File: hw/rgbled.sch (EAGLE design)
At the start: 14 parts, among them IC1 LE33CZ, Q1 IRLZ34N, Q2 IRLZ34N, Q3 IRLZ34N, U1 ATTINY85-20P, X1 22-23-2021

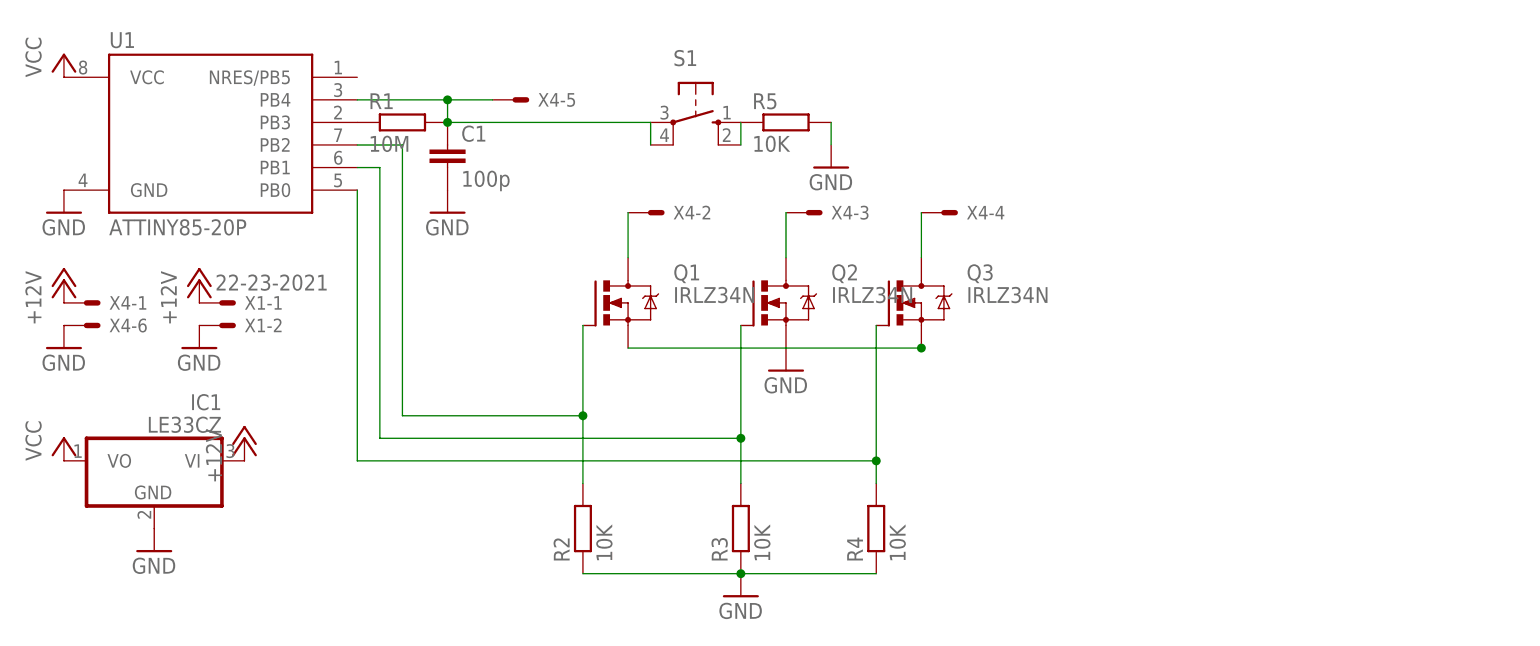
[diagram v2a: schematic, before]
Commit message: upravy problikavani
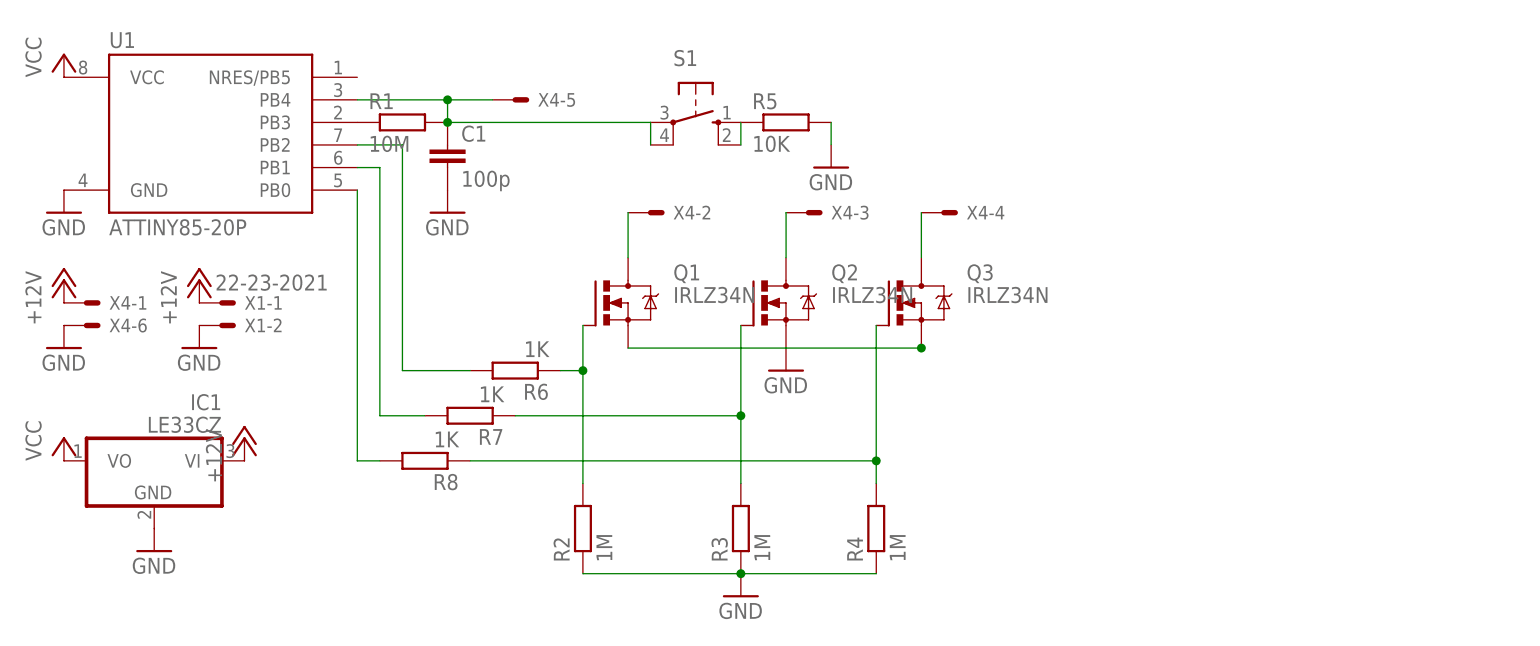
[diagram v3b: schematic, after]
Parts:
- added R6, R7, R8: 1K, resistor:R-EU_0204/5
- R2, R3, R4: value 10K -> 1M
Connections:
- new net N$6: Q1.G, R2.2, R6.1
- new net N$8: Q2.G, R3.2, R7.1
- new net N$9: Q3.G, R4.2, R8.1
- net N$10: now also R8.2; no longer Q3.G, R4.2
- net N$11: now also R7.2; no longer Q2.G, R3.2
- net N$12: now also R6.2; no longer Q1.G, R2.2
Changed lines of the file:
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@@
 <part name="C1" library="resistor" deviceset="C-EU" device="025-024X044" value="100p"/>
 <part name="GND6" library="supply1" deviceset="GND" device=""/>
-<part name="R2" library="resistor" deviceset="R-EU_" device="0204/5" value="10K"/>
-<part name="R3" library="resistor" deviceset="R-EU_" device="0204/5" value="10K"/>
-<part name="R4" library="resistor" deviceset="R-EU_" device="0204/5" value="10K"/>
+<part name="R2" library="resistor" deviceset="R-EU_" device="0204/5" value="1M"/>
+<part name="R3" library="resistor" deviceset="R-EU_" device="0204/5" value="1M"/>
+<part name="R4" library="resistor" deviceset="R-EU_" device="0204/5" value="1M"/>
 <part name="GND7" library="supply1" deviceset="GND" device=""/>
 <part name="S1" library="switch-omron" deviceset="10-XX" device=""/>
 <part name="GND8" library="supply1" deviceset="GND" device=""/>
 <part name="R5" library="resistor" deviceset="R-EU_" device="0204/5" value="10K"/>
+<part name="R6" library="resistor" deviceset="R-EU_" device="0204/5" value="1K"/>
+<part name="R7" library="resistor" deviceset="R-EU_" device="0204/5" value="1K"/>
+<part name="R8" library="resistor" deviceset="R-EU_" device="0204/5" value="1K"/>
 </parts>
 <sheets>
@@
 <instance part="GND8" gate="1" x="93.98" y="53.34"/>
 <instance part="R5" gate="G$1" x="88.9" y="58.42"/>
+<instance part="R6" gate="G$1" x="58.42" y="30.48" rot="R180"/>
+<instance part="R7" gate="G$1" x="53.34" y="25.4" rot="R180"/>
+<instance part="R8" gate="G$1" x="48.26" y="20.32" rot="R180"/>
 </instances>
 <busses>
@@
 <net name="N$10" class="0">
 <segment>
-<pinref part="Q3" gate="G$1" pin="G"/>
-<wire x1="99.06" y1="35.56" x2="99.06" y2="20.32" width="0.1524" layer="91"/>
-<pinref part="R4" gate="G$1" pin="2"/>
 <pinref part="U1" gate="G$1" pin="PB0"/>
-<wire x1="99.06" y1="20.32" x2="99.06" y2="17.78" width="0.1524" layer="91"/>
-<wire x1="99.06" y1="20.32" x2="40.64" y2="20.32" width="0.1524" layer="91"/>
 <wire x1="40.64" y1="20.32" x2="40.64" y2="50.8" width="0.1524" layer="91"/>
-<junction x="99.06" y="20.32"/>
+<pinref part="R8" gate="G$1" pin="2"/>
+<wire x1="40.64" y1="20.32" x2="43.18" y2="20.32" width="0.1524" layer="91"/>
 </segment>
 </net>
 <net name="N$11" class="0">
 <segment>
-<pinref part="Q2" gate="G$1" pin="G"/>
-<wire x1="83.82" y1="35.56" x2="83.82" y2="22.86" width="0.1524" layer="91"/>
-<pinref part="R3" gate="G$1" pin="2"/>
-<wire x1="83.82" y1="22.86" x2="83.82" y2="17.78" width="0.1524" layer="91"/>
-<wire x1="83.82" y1="22.86" x2="43.18" y2="22.86" width="0.1524" layer="91"/>
-<wire x1="43.18" y1="22.86" x2="43.18" y2="53.34" width="0.1524" layer="91"/>
 <pinref part="U1" gate="G$1" pin="PB1"/>
 <wire x1="43.18" y1="53.34" x2="40.64" y2="53.34" width="0.1524" layer="91"/>
-<junction x="83.82" y="22.86"/>
+<wire x1="43.18" y1="53.34" x2="43.18" y2="25.4" width="0.1524" layer="91"/>
+<pinref part="R7" gate="G$1" pin="2"/>
+<wire x1="43.18" y1="25.4" x2="48.26" y2="25.4" width="0.1524" layer="91"/>
 </segment>
 </net>
 <net name="N$12" class="0">
 <segment>
-<pinref part="Q1" gate="G$1" pin="G"/>
-<wire x1="66.04" y1="35.56" x2="66.04" y2="25.4" width="0.1524" layer="91"/>
-<pinref part="R2" gate="G$1" pin="2"/>
-<wire x1="66.04" y1="25.4" x2="66.04" y2="17.78" width="0.1524" layer="91"/>
-<wire x1="66.04" y1="25.4" x2="45.72" y2="25.4" width="0.1524" layer="91"/>
-<wire x1="45.72" y1="25.4" x2="45.72" y2="55.88" width="0.1524" layer="91"/>
 <pinref part="U1" gate="G$1" pin="PB2"/>
 <wire x1="45.72" y1="55.88" x2="40.64" y2="55.88" width="0.1524" layer="91"/>
-<junction x="66.04" y="25.4"/>
+<wire x1="45.72" y1="55.88" x2="45.72" y2="30.48" width="0.1524" layer="91"/>
+<pinref part="R6" gate="G$1" pin="2"/>
+<wire x1="45.72" y1="30.48" x2="53.34" y2="30.48" width="0.1524" layer="91"/>
 </segment>
 </net>
@@
 </segment>
 </net>
+<net name="N$8" class="0">
+<segment>
+<pinref part="Q2" gate="G$1" pin="G"/>
+<wire x1="83.82" y1="35.56" x2="83.82" y2="25.4" width="0.1524" layer="91"/>
+<pinref part="R3" gate="G$1" pin="2"/>
+<pinref part="R7" gate="G$1" pin="1"/>
+<wire x1="83.82" y1="25.4" x2="83.82" y2="17.78" width="0.1524" layer="91"/>
+<wire x1="58.42" y1="25.4" x2="83.82" y2="25.4" width="0.1524" layer="91"/>
+<junction x="83.82" y="25.4"/>
+</segment>
+</net>
+<net name="N$9" class="0">
+<segment>
+<pinref part="Q3" gate="G$1" pin="G"/>
+<wire x1="99.06" y1="35.56" x2="99.06" y2="20.32" width="0.1524" layer="91"/>
+<pinref part="R4" gate="G$1" pin="2"/>
+<pinref part="R8" gate="G$1" pin="1"/>
+<wire x1="99.06" y1="20.32" x2="99.06" y2="17.78" width="0.1524" layer="91"/>
+<wire x1="53.34" y1="20.32" x2="99.06" y2="20.32" width="0.1524" layer="91"/>
+<junction x="99.06" y="20.32"/>
+</segment>
+</net>
+<net name="N$6" class="0">
+<segment>
+<pinref part="Q1" gate="G$1" pin="G"/>
+<pinref part="R2" gate="G$1" pin="2"/>
+<wire x1="66.04" y1="35.56" x2="66.04" y2="30.48" width="0.1524" layer="91"/>
+<pinref part="R6" gate="G$1" pin="1"/>
+<wire x1="66.04" y1="30.48" x2="66.04" y2="17.78" width="0.1524" layer="91"/>
+<wire x1="63.5" y1="30.48" x2="66.04" y2="30.48" width="0.1524" layer="91"/>
+<junction x="66.04" y="30.48"/>
+</segment>
+</net>

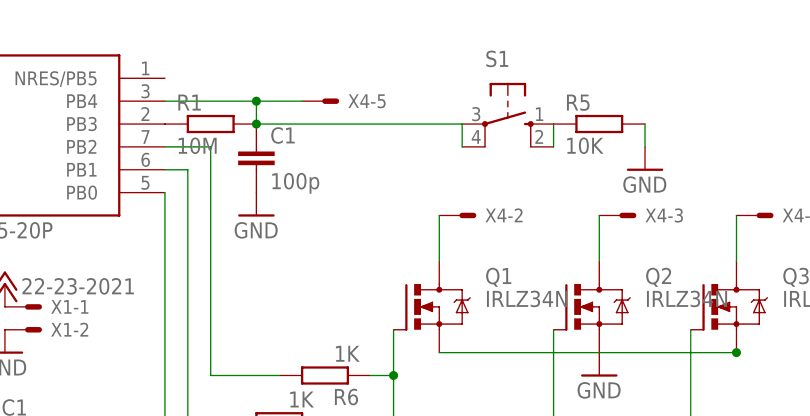
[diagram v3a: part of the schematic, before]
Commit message: vyhozen dotykovy senzor
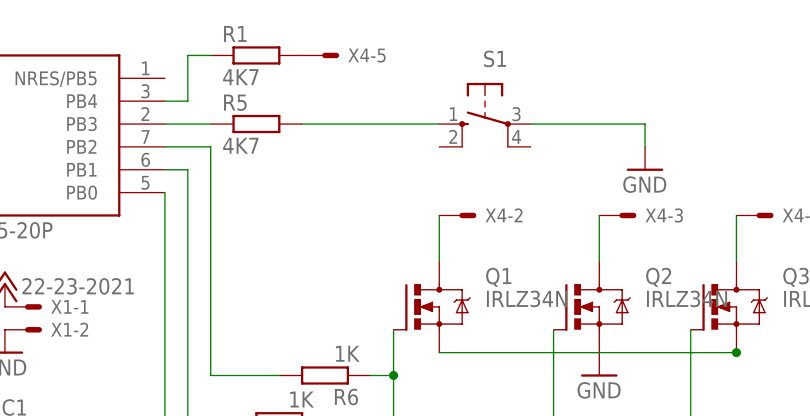
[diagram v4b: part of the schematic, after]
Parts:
- removed C1: 100p, resistor:C-EU025-024X044
- R1: value 10M -> 4K7
- R5: value 10K -> 4K7
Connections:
- removed net N$7: C1.1, R1.2, S1.P, S1.P1, U1.PB4, X4-5.S
- new net N$13: R1.2, X4-5.S
- new net N$14: R5.1, U1.PB3
- net GND: now also S1.P; no longer C1.2, R5.2
- net N$1: now also R5.2; no longer R5.1, S1.S1
- net N$5: now also U1.PB4; no longer U1.PB3
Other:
- moved on the sheet: R1, R5, S1, X4-5
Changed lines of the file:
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@@
 <part name="P+5" library="supply1" deviceset="+12V" device=""/>
 <part name="GND5" library="supply1" deviceset="GND" device=""/>
-<part name="R1" library="resistor" deviceset="R-EU_" device="0204/5" value="10M"/>
-<part name="C1" library="resistor" deviceset="C-EU" device="025-024X044" value="100p"/>
-<part name="GND6" library="supply1" deviceset="GND" device=""/>
 <part name="R2" library="resistor" deviceset="R-EU_" device="0204/5" value="1M"/>
 <part name="R3" library="resistor" deviceset="R-EU_" device="0204/5" value="1M"/>
@@
 <part name="S1" library="switch-omron" deviceset="10-XX" device=""/>
 <part name="GND8" library="supply1" deviceset="GND" device=""/>
-<part name="R5" library="resistor" deviceset="R-EU_" device="0204/5" value="10K"/>
+<part name="R5" library="resistor" deviceset="R-EU_" device="0204/5" value="4K7"/>
 <part name="R6" library="resistor" deviceset="R-EU_" device="0204/5" value="1K"/>
 <part name="R7" library="resistor" deviceset="R-EU_" device="0204/5" value="1K"/>
 <part name="R8" library="resistor" deviceset="R-EU_" device="0204/5" value="1K"/>
+<part name="R1" library="resistor" deviceset="R-EU_" device="0204/5" value="4K7"/>
 </parts>
 <sheets>
@@
 <instance part="X4" gate="-3" x="91.44" y="48.26"/>
 <instance part="X4" gate="-4" x="106.68" y="48.26"/>
-<instance part="X4" gate="-5" x="58.42" y="60.96"/>
+<instance part="X4" gate="-5" x="58.42" y="66.04"/>
 <instance part="X4" gate="-6" x="10.16" y="35.56"/>
 <instance part="GND1" gate="1" x="22.86" y="33.02"/>
@@
 <instance part="P+5" gate="1" x="7.62" y="40.64"/>
 <instance part="GND5" gate="1" x="7.62" y="33.02"/>
-<instance part="R1" gate="G$1" x="45.72" y="58.42"/>
-<instance part="C1" gate="G$1" x="50.8" y="55.88"/>
-<instance part="GND6" gate="1" x="50.8" y="48.26"/>
 <instance part="R2" gate="G$1" x="66.04" y="12.7" rot="R90"/>
 <instance part="R3" gate="G$1" x="83.82" y="12.7" rot="R90"/>
 <instance part="R4" gate="G$1" x="99.06" y="12.7" rot="R90"/>
 <instance part="GND7" gate="1" x="83.82" y="5.08"/>
-<instance part="S1" gate="1" x="78.74" y="58.42" rot="R270"/>
+<instance part="S1" gate="1" x="76.2" y="58.42" rot="MR270"/>
 <instance part="GND8" gate="1" x="93.98" y="53.34"/>
-<instance part="R5" gate="G$1" x="88.9" y="58.42"/>
+<instance part="R5" gate="G$1" x="50.8" y="58.42"/>
 <instance part="R6" gate="G$1" x="58.42" y="30.48" rot="R180"/>
 <instance part="R7" gate="G$1" x="53.34" y="25.4" rot="R180"/>
 <instance part="R8" gate="G$1" x="48.26" y="20.32" rot="R180"/>
+<instance part="R1" gate="G$1" x="50.8" y="66.04"/>
 </instances>
 <busses>
@@
 </segment>
 <segment>
-<pinref part="C1" gate="G$1" pin="2"/>
-<pinref part="GND6" gate="1" pin="GND"/>
-</segment>
-<segment>
 <pinref part="R2" gate="G$1" pin="1"/>
 <pinref part="R3" gate="G$1" pin="1"/>
@@
 </segment>
 <segment>
-<pinref part="R5" gate="G$1" pin="2"/>
 <pinref part="GND8" gate="1" pin="GND"/>
 <wire x1="93.98" y1="58.42" x2="93.98" y2="55.88" width="0.1524" layer="91"/>
+<pinref part="S1" gate="1" pin="P"/>
+<wire x1="81.28" y1="58.42" x2="93.98" y2="58.42" width="0.1524" layer="91"/>
 </segment>
 </net>
@@
 <pinref part="Q3" gate="G$1" pin="D"/>
 <wire x1="104.14" y1="48.26" x2="104.14" y2="43.18" width="0.1524" layer="91"/>
-</segment>
-</net>
-<net name="N$5" class="0">
-<segment>
-<pinref part="U1" gate="G$1" pin="PB3"/>
-<pinref part="R1" gate="G$1" pin="1"/>
 </segment>
 </net>
@@
 <pinref part="R6" gate="G$1" pin="2"/>
 <wire x1="45.72" y1="30.48" x2="53.34" y2="30.48" width="0.1524" layer="91"/>
-</segment>
-</net>
-<net name="N$7" class="0">
-<segment>
-<pinref part="R1" gate="G$1" pin="2"/>
-<pinref part="C1" gate="G$1" pin="1"/>
-<pinref part="X4" gate="-5" pin="S"/>
-<pinref part="U1" gate="G$1" pin="PB4"/>
-<wire x1="40.64" y1="60.96" x2="50.8" y2="60.96" width="0.1524" layer="91"/>
-<wire x1="50.8" y1="60.96" x2="55.88" y2="60.96" width="0.1524" layer="91"/>
-<wire x1="50.8" y1="60.96" x2="50.8" y2="58.42" width="0.1524" layer="91"/>
-<pinref part="S1" gate="1" pin="P"/>
-<wire x1="50.8" y1="58.42" x2="73.66" y2="58.42" width="0.1524" layer="91"/>
-<pinref part="S1" gate="1" pin="P1"/>
-<wire x1="73.66" y1="58.42" x2="73.66" y2="55.88" width="0.1524" layer="91"/>
-<junction x="50.8" y="60.96"/>
-<junction x="50.8" y="58.42"/>
-</segment>
-</net>
-<net name="N$1" class="0">
-<segment>
-<pinref part="S1" gate="1" pin="S"/>
-<pinref part="R5" gate="G$1" pin="1"/>
-<pinref part="S1" gate="1" pin="S1"/>
-<wire x1="83.82" y1="58.42" x2="83.82" y2="55.88" width="0.1524" layer="91"/>
 </segment>
 </net>
@@
 </segment>
 </net>
+<net name="N$5" class="0">
+<segment>
+<pinref part="U1" gate="G$1" pin="PB4"/>
+<pinref part="R1" gate="G$1" pin="1"/>
+<wire x1="40.64" y1="60.96" x2="43.18" y2="60.96" width="0.1524" layer="91"/>
+<wire x1="43.18" y1="60.96" x2="43.18" y2="66.04" width="0.1524" layer="91"/>
+<wire x1="43.18" y1="66.04" x2="45.72" y2="66.04" width="0.1524" layer="91"/>
+</segment>
+</net>
+<net name="N$13" class="0">
+<segment>
+<pinref part="R1" gate="G$1" pin="2"/>
+<pinref part="X4" gate="-5" pin="S"/>
+</segment>
+</net>
+<net name="N$14" class="0">
+<segment>
+<pinref part="U1" gate="G$1" pin="PB3"/>
+<pinref part="R5" gate="G$1" pin="1"/>
+<wire x1="40.64" y1="58.42" x2="45.72" y2="58.42" width="0.1524" layer="91"/>
+</segment>
+</net>
+<net name="N$1" class="0">
+<segment>
+<pinref part="S1" gate="1" pin="S"/>
+<pinref part="R5" gate="G$1" pin="2"/>
+<wire x1="55.88" y1="58.42" x2="71.12" y2="58.42" width="0.1524" layer="91"/>
+</segment>
+</net>
